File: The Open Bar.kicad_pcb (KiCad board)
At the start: 2 copper layers, 76.2 x 101.6 mm, 61 parts, among them IC1 MCP23008, IC2 MCP23008, IC3 MCP23008, IC4 MCP23008, P1 CONN_01X02, P2 CONN_01X02, P3 CONN_01X02, P4 CONN_01X02, P5 CONN_01X02, P6 CONN_01X16, P7 CONN_01X16, P8 CONN_01X16, P9 CONN_01X16, Q1 MTM232270LBF, Q10 MTM232270LBF, Q11 MTM232270LBF, Q12 MTM232270LBF, Q13 MTM232270LBF, Q14 MTM232270LBF, Q15 MTM232270LBF, Q16 MTM232270LBF, Q17 MTM232270LBF, Q18 MTM232270LBF, Q19 MTM232270LBF, Q2 MTM232270LBF, Q20 MTM232270LBF, Q21 MTM232270LBF, Q22 MTM232270LBF, Q23 MTM232270LBF, Q24 MTM232270LBF, Q25 MTM232270LBF, Q26 MTM232270LBF, Q27 MTM232270LBF, Q28 MTM232270LBF, Q29 MTM232270LBF, Q3 MTM232270LBF, Q30 MTM232270LBF, Q31 MTM232270LBF, Q32 MTM232270LBF, Q4 MTM232270LBF, Q5 MTM232270LBF, Q6 MTM232270LBF, Q7 MTM232270LBF, Q8 MTM232270LBF, Q9 MTM232270LBF, U1 AP3003-5.0V, U2 TC1262

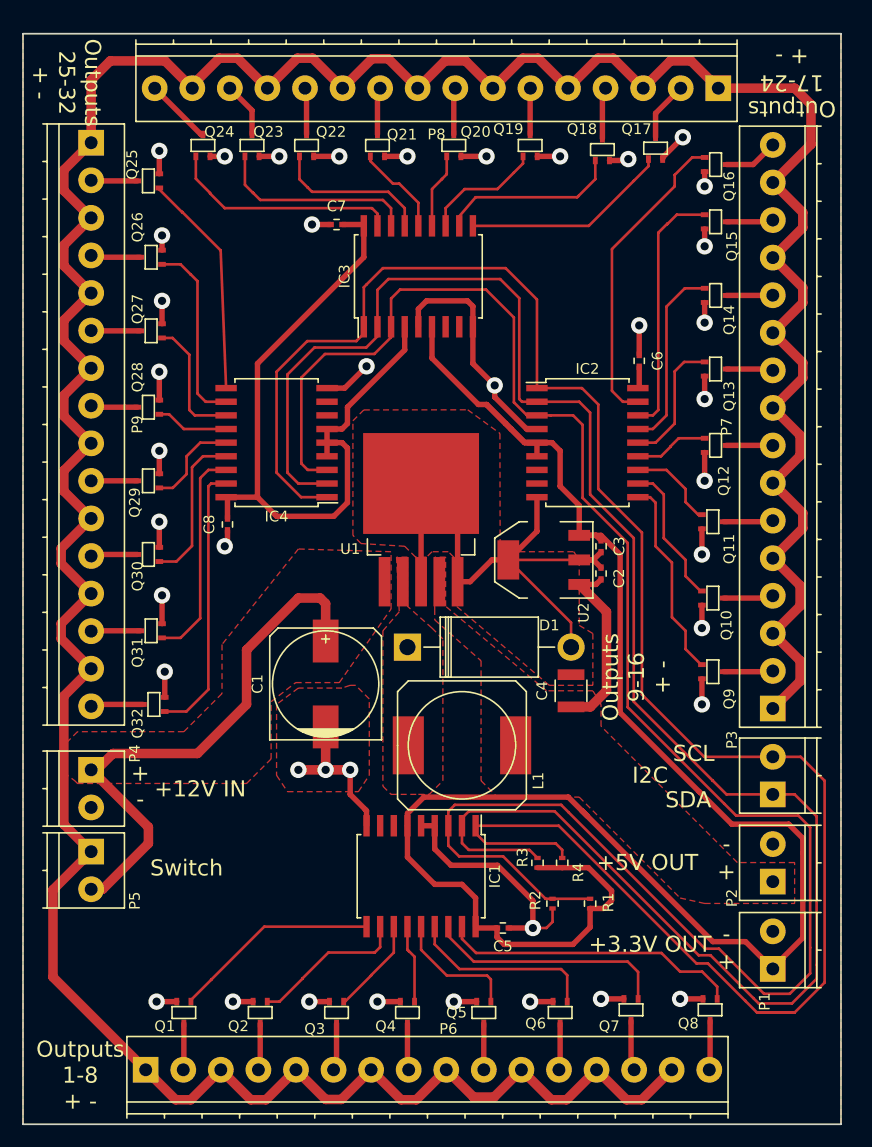
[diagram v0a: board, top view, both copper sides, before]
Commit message: Rev B, Added Flywheel Diodes
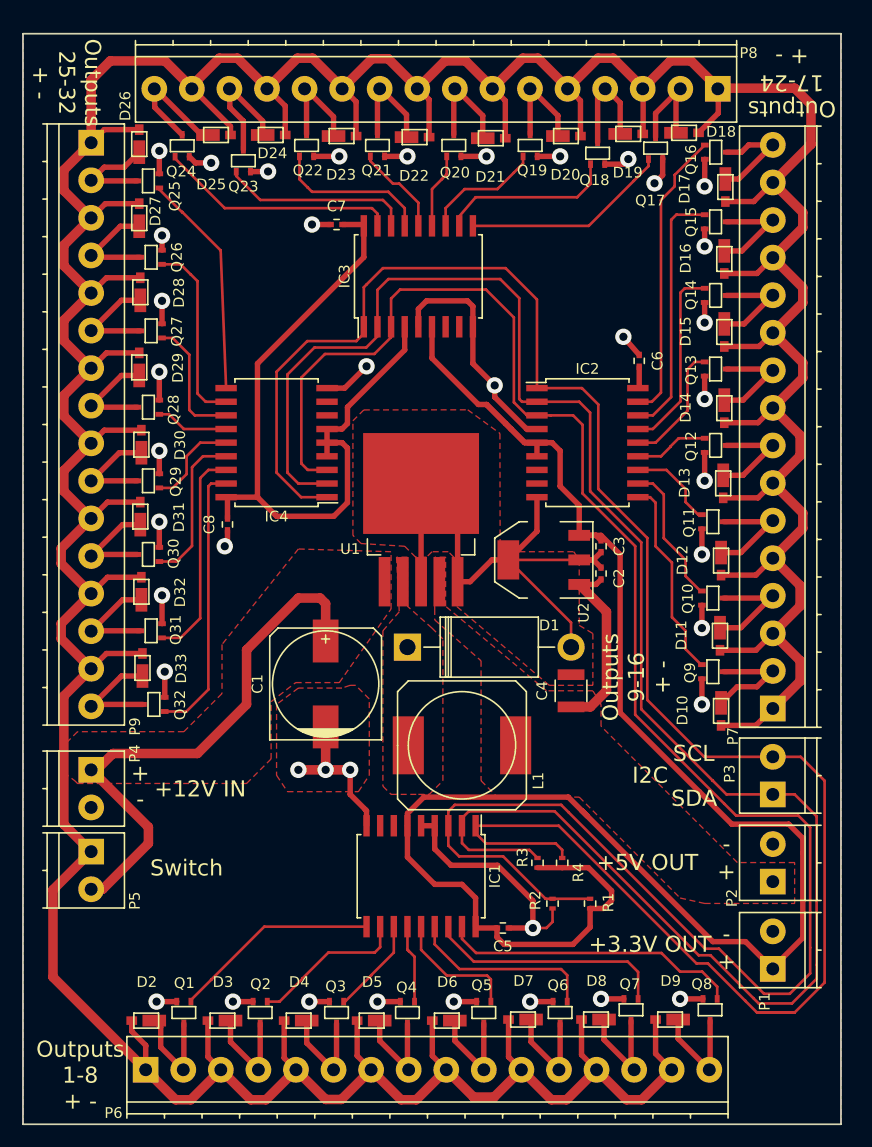
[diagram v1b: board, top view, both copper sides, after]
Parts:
- added D10: D_Schottky, Project Folder:microSMP, F.Cu at (180.6, 111.7)
- added D11: D_Schottky, Project Folder:microSMP, F.Cu at (180.5, 104.7)
- added D12: D_Schottky, Project Folder:microSMP, F.Cu at (180.6, 97.7)
- added D13: D_Schottky, Project Folder:microSMP, F.Cu at (180.8, 90.5)
- added D14: D_Schottky, Project Folder:microSMP, F.Cu at (180.9, 83.5)
- added D15: D_Schottky, Project Folder:microSMP, F.Cu at (180.9, 76.4)
- added D16: D_Schottky, Project Folder:microSMP, F.Cu at (180.9, 69.6)
- added D17: D_Schottky, Project Folder:microSMP, F.Cu at (181.0, 62.9)
- added D18: D_Schottky, Project Folder:microSMP, F.Cu at (177.5, 57.5)
- added D19: D_Schottky, Project Folder:microSMP, F.Cu at (172.3, 57.6)
- added D2: D_Schottky, Project Folder:microSMP, F.Cu at (126.7, 140.2)
- added D20: D_Schottky, Project Folder:microSMP, F.Cu at (166.5, 57.8)
- added D21: D_Schottky, Project Folder:microSMP, F.Cu at (159.5, 58.0)
- added D22: D_Schottky, Project Folder:microSMP, F.Cu at (152.4, 57.9)
- added D23: D_Schottky, Project Folder:microSMP, F.Cu at (145.6, 57.8)
- added D24: D_Schottky, Project Folder:microSMP, F.Cu at (139.0, 57.7)
- added D25: D_Schottky, Project Folder:microSMP, F.Cu at (133.9, 57.7)
- added D26: D_Schottky, Project Folder:microSMP, F.Cu at (126.4, 58.2)
- added D27: D_Schottky, Project Folder:microSMP, F.Cu at (126.4, 65.1)
- added D28: D_Schottky, Project Folder:microSMP, F.Cu at (126.5, 72.0)
- added D29: D_Schottky, Project Folder:microSMP, F.Cu at (126.4, 79.0)
- added D3: D_Schottky, Project Folder:microSMP, F.Cu at (133.8, 140.2)
- added D30: D_Schottky, Project Folder:microSMP, F.Cu at (126.6, 86.2)
- added D31: D_Schottky, Project Folder:microSMP, F.Cu at (126.5, 92.9)
- added D32: D_Schottky, Project Folder:microSMP, F.Cu at (126.6, 99.9)
- added D33: D_Schottky, Project Folder:microSMP, F.Cu at (126.7, 107.0)
- added D4: D_Schottky, Project Folder:microSMP, F.Cu at (140.9, 140.2)
- added D5: D_Schottky, Project Folder:microSMP, F.Cu at (147.7, 140.2)
- added D6: D_Schottky, Project Folder:microSMP, F.Cu at (154.7, 140.2)
- added D7: D_Schottky, Project Folder:microSMP, F.Cu at (161.8, 140.1)
- added D8: D_Schottky, Project Folder:microSMP, F.Cu at (168.6, 140.1)
- added D9: D_Schottky, Project Folder:microSMP, F.Cu at (175.5, 140.1)
- moved Q24 1.93 mm to (130.4, 58.7)
- moved Q23 1.64 mm to (136.1, 60.1)
- moved Q16 1.15 mm to (180.1, 59.3)
- moved Q18 0.56 mm to (169.1, 59.4)
- moved P8 0.07 mm to (180.3, 53.4)
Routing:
- net +12V: track 338.2 -> 503.0 mm
- net Net-(D24-Pad2): track 5.17 -> 11.9 mm
- net Net-(D11-Pad2): track 4.66 -> 10.8 mm
- net Net-(D10-Pad2): track 4.60 -> 10.7 mm
- net Net-(D12-Pad2): track 4.61 -> 10.7 mm
- net Net-(D33-Pad2): track 4.90 -> 10.8 mm
- net Net-(D32-Pad2): track 4.59 -> 10.5 mm
- net Net-(D25-Pad2): track 6.28 -> 12.2 mm
- net Net-(D9-Pad2): track 4.60 -> 10.5 mm
- net Net-(D8-Pad2): track 4.69 -> 10.5 mm
- net Net-(D31-Pad2): track 4.38 -> 10.2 mm
- net Net-(D19-Pad2): track 4.82 -> 10.6 mm
- net Net-(D13-Pad2): track 4.32 -> 10.1 mm
- net Net-(D30-Pad2): track 4.32 -> 10.1 mm
- net Net-(D7-Pad2): track 4.36 -> 10.1 mm
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
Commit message: Added Fiducials and Fixed Diode Orientation
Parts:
- added FID1: Fiducial_Modern_CopperTop, Fiducials:Fiducial_1mm_Dia_2.54mm_Outer_CopperTop, F.Cu at (138.0, 68.9)
- added FID2: Fiducial_Modern_CopperTop, Fiducials:Fiducial_1mm_Dia_2.54mm_Outer_CopperTop, F.Cu at (123.4, 135.0)
- added FID3: Fiducial_Modern_CopperTop, Fiducials:Fiducial_1mm_Dia_2.54mm_Outer_CopperTop, F.Cu at (186.4, 144.3)
- added REF***: OSHW-Logo_5.7x6mm_SilkScreen, Symbols:OSHW-Logo_5.7x6mm_SilkScreen, F.Cu at (141.0, 124.4)
- moved D10 1.58 mm to (181.1, 110.2), turned to 90 degrees
- moved D8 1.08 mm to (169.6, 140.5), turned to 0 degrees
- moved D9 1.04 mm to (176.5, 140.4), turned to 0 degrees
- moved D26 1.02 mm to (126.2, 59.2), turned to 270 degrees
- moved D11 0.94 mm to (181.0, 103.9), turned to 90 degrees
- moved D14 0.92 mm to (181.1, 82.6), turned to 90 degrees
- moved D29 0.91 mm to (126.3, 79.9), turned to 270 degrees
- moved D28 0.90 mm to (126.5, 72.9), turned to 270 degrees
- moved D6 0.85 mm to (155.5, 140.5), turned to 0 degrees
- moved D17 0.82 mm to (181.2, 62.1), turned to 90 degrees
- moved D4 0.82 mm to (141.7, 140.4), turned to 0 degrees
- moved D19 0.81 mm to (171.5, 57.5), turned to 180 degrees
- moved D12 0.81 mm to (180.7, 96.9), turned to 90 degrees
- moved D31 0.81 mm to (126.4, 93.7), turned to 270 degrees
- moved D32 0.81 mm to (126.5, 100.7), turned to 270 degrees
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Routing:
- net +12V: track 503.0 -> 488.9 mm
- net Net-(D18-Pad2): track 9.88 -> 5.18 mm
- net Net-(D10-Pad2): track 10.7 -> 9.57 mm
- net Net-(D11-Pad2): track 10.8 -> 10.0 mm
- net Net-(D8-Pad2): track 10.5 -> 9.76 mm
- net Net-(D9-Pad2): track 10.5 -> 9.81 mm
- net Net-(D7-Pad2): track 10.1 -> 9.51 mm
- net Net-(D6-Pad2): track 10.0 -> 9.43 mm
- net Net-(D26-Pad2): track 9.91 -> 9.33 mm
- net Net-(D33-Pad2): track 10.8 -> 10.3 mm
- net Net-(D13-Pad2): track 10.1 -> 9.54 mm
- net Net-(D16-Pad2): track 10.1 -> 9.55 mm
- net Net-(D14-Pad2): track 10.0 -> 9.51 mm
- net Net-(D25-Pad2): track 12.2 -> 11.6 mm
- net Net-(D30-Pad2): track 10.1 -> 9.58 mm

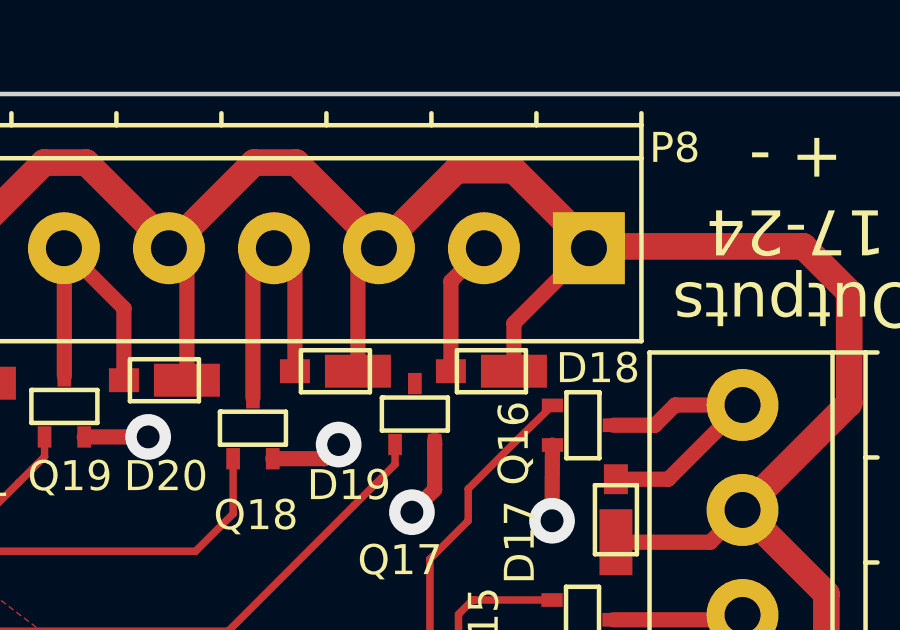
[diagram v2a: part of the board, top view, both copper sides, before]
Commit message: Fix Unconnected Mosfet on PCB
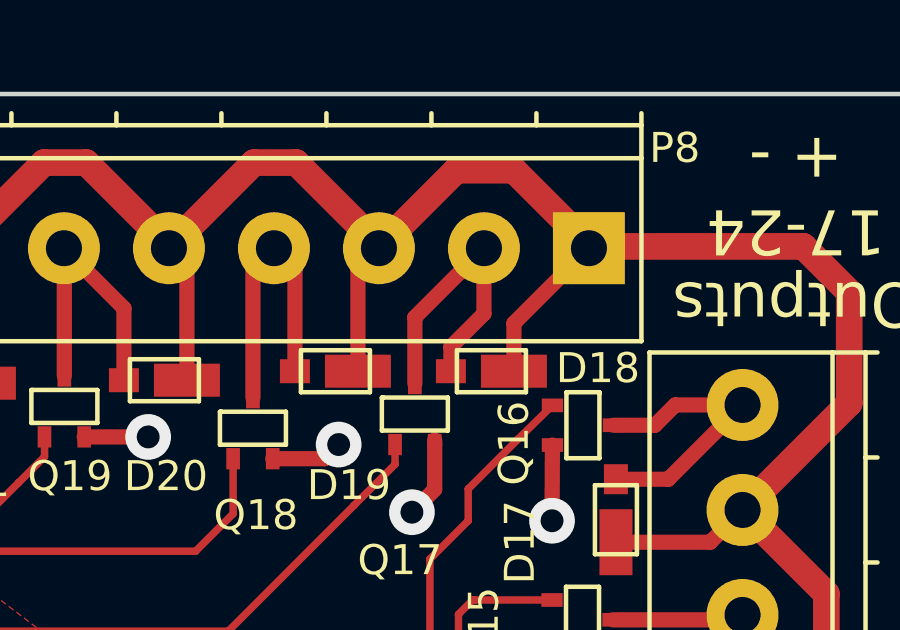
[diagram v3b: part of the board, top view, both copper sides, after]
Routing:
- net Net-(D18-Pad2): track 5.18 -> 10.0 mm
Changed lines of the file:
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@@
   (general
     (links 266)
-    (no_connects 4)
+    (no_connects 3)
     (area 112.863094 46.275 196.936906 151.755)
     (thickness 1.6)
     (drawings 18)
-    (tracks 820)
+    (tracks 822)
     (zones 0)
     (modules 97)
@@
   (title_block
     (title "The Open Bar I/O Board")
-    (date 2017-03-21)
-    (rev C)
+    (date 2017-04-11)
+    (rev D)
     (company "The Open Bar")
   )
@@
   )
   (setup
-    (last_trace_width 0.25)
+    (last_trace_width 0.508)
     (user_trace_width 0.508)
     (user_trace_width 0.889)
@@
       (padsonsilk false)
       (subtractmaskfromsilk false)
-      (outputformat 4)
+      (outputformat 1)
       (mirror false)
       (drillshape 0)
       (scaleselection 1)
-      (outputdirectory PDFs/))
+      (outputdirectory Gerbers/))
   )
   (net 0 "")
@@
   (segment (start 182.5 59.3) (end 181.116 59.3) (width 0.508) (layer F.Cu) (net 58) (status 20))
   (segment (start 183.175 58.625) (end 182.5 59.3) (width 0.508) (layer F.Cu) (net 58))
-  (segment (start 175.7 54.5) (end 176.8 53.4) (width 0.508) (layer F.Cu) (net 59))
-  (segment (start 175.7 57.5) (end 175.7 54.5) (width 0.508) (layer F.Cu) (net 59))
-  (segment (start 176.4 53.78) (end 176.84 53.34) (width 0.508) (layer F.Cu) (net 59))
+  (segment (start 174.498 57.912) (end 174.498 55.702) (width 0.508) (layer F.Cu) (net 59) (status 400000))
+  (segment (start 174.498 55.702) (end 176.8 53.4) (width 0.508) (layer F.Cu) (net 59) (status 800000))
+  (segment (start 175.7 57.5) (end 175.7 56.6846) (width 0.508) (layer F.Cu) (net 59) (status 400000))
+  (segment (start 176.8 55.5846) (end 176.8 53.4) (width 0.508) (layer F.Cu) (net 59) (status 800000))
+  (segment (start 175.7 56.6846) (end 176.8 55.5846) (width 0.508) (layer F.Cu) (net 59))
   (segment (start 170.5 57.5) (end 170.5 54.1) (width 0.508) (layer F.Cu) (net 60))
   (segment (start 170.5 54.1) (end 169.8 53.4) (width 0.508) (layer F.Cu) (net 60))
